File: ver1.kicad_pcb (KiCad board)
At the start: 2 copper layers, 103 x 76 mm, 61 parts, among them P1 CONN_6, P2 CONN_2, P3 CONN_4, P4 CONN_4, P5 CONN_4, P6 USB_Micro_B, U1 MCP1790, U2 STM32F100C6, U3 DRV8833C, U4 DRV8833C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

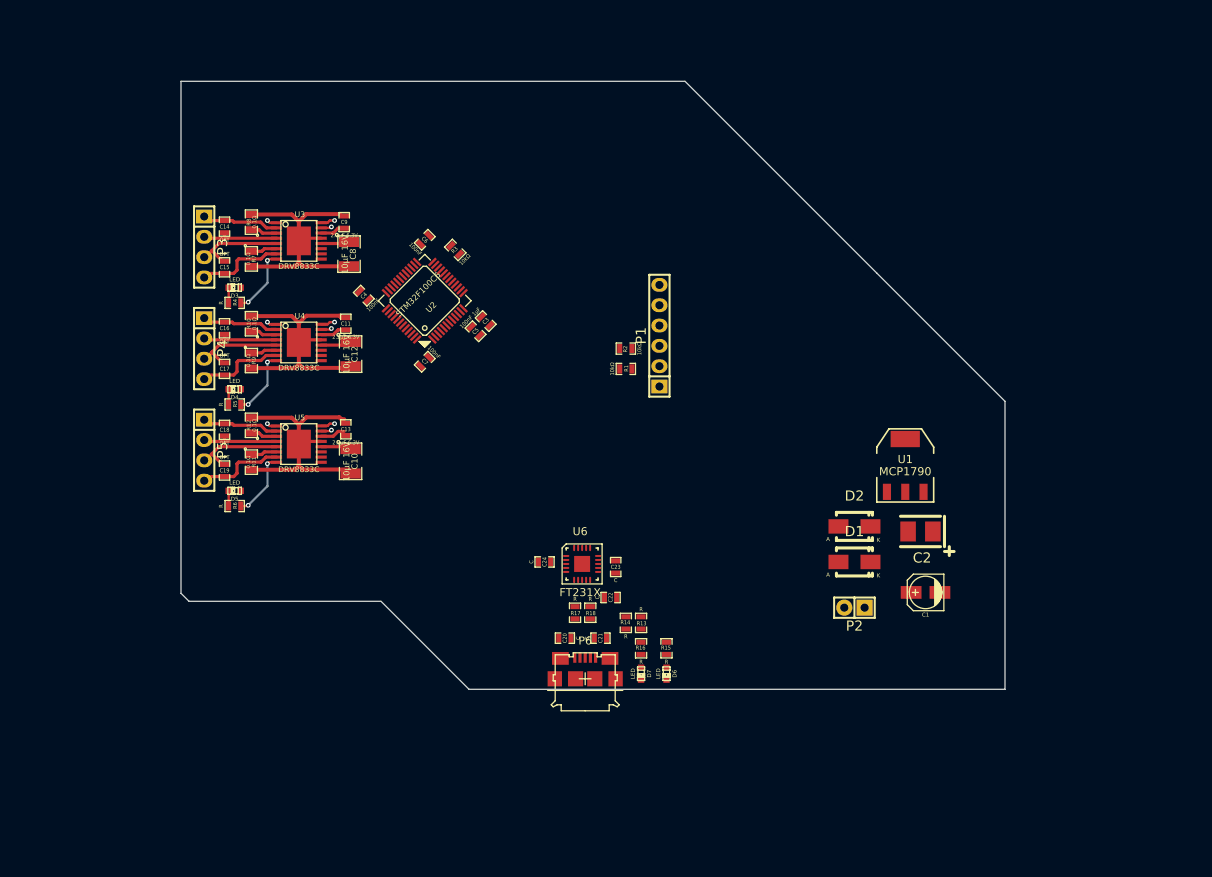
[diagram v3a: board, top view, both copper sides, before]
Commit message: Added PC interface and did some routing
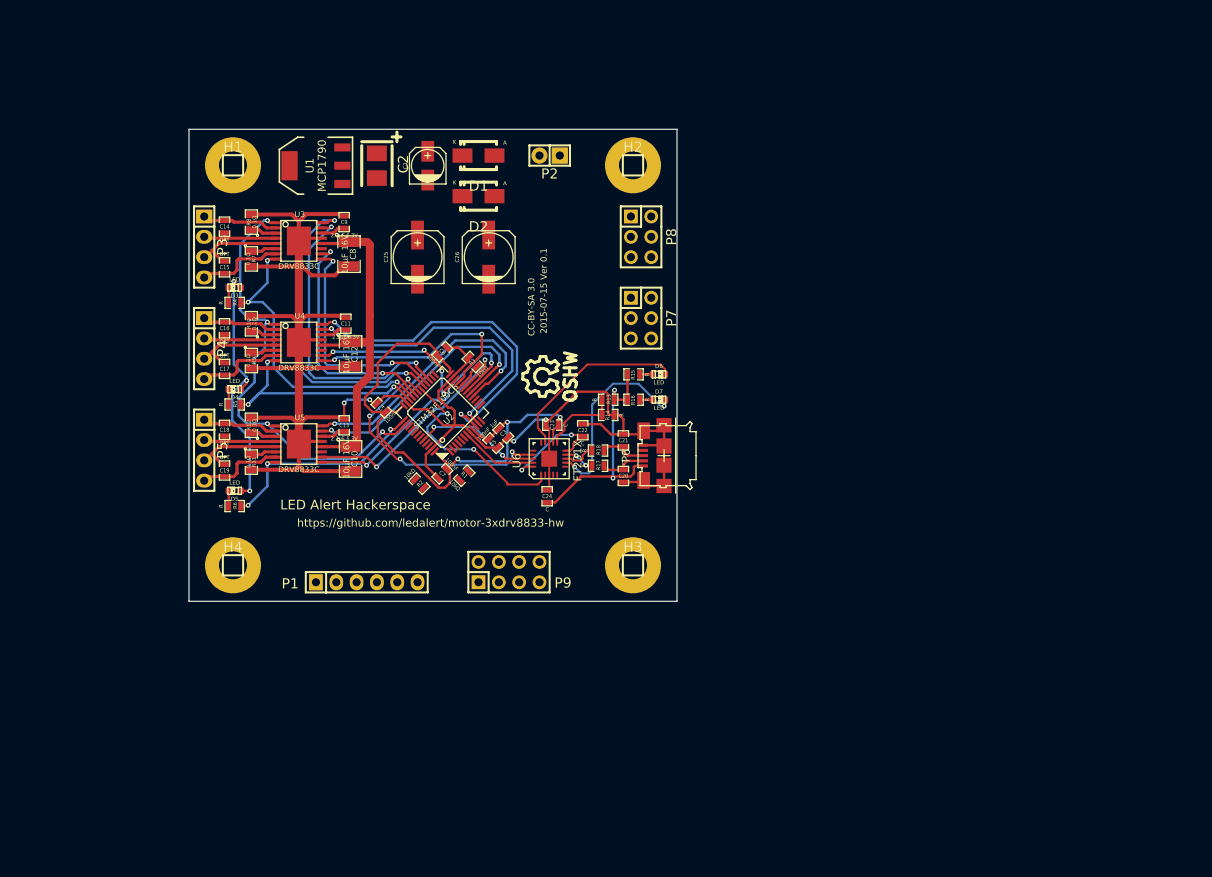
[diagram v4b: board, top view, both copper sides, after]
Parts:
- added C25: 220µF 16V, Capacitors_SMD:c_elec_6.3x7.7, F.Cu at (115.6, 94.0)
- added C26: 220µF 16V, Capacitors_SMD:c_elec_6.3x7.7, F.Cu at (124.5, 94.0)
- added H1: CONN_1, Pin_Headers:Pin_Header_Straight_1x01, F.Cu at (92.5, 82.5)
- added H2: CONN_1, Pin_Headers:Pin_Header_Straight_1x01, F.Cu at (142.5, 82.5)
- added H3: CONN_1, Pin_Headers:Pin_Header_Straight_1x01, F.Cu at (142.5, 132.5)
- added H4: CONN_1, Pin_Headers:Pin_Header_Straight_1x01, F.Cu at (92.5, 132.5)
- added P7: CONN_3X2, Pin_Headers:Pin_Header_Straight_2x03, F.Cu at (143.5, 101.6)
- added P8: CONN_3X2, Pin_Headers:Pin_Header_Straight_2x03, F.Cu at (143.5, 91.4)
- added P9: CONN_4X2, Pin_Headers:Pin_Header_Straight_2x04, F.Cu at (127.0, 133.3)
- added SYM: Symbol_OSHW-Logo_SilkScreen_07Jul2012, Symbols:Symbol_OSHW-Logo_SilkScreen, F.Cu at (131.2, 108.9)
- moved U1 82.6 mm to (102.9, 82.5), turned to 90 degrees
- moved C1 82.0 mm to (116.8, 82.5), turned to 90 degrees
- moved C2 81.9 mm to (110.5, 82.5), turned to 270 degrees
- moved D1 69.2 mm to (123.2, 81.3), turned to 180 degrees
- moved P2 68.2 mm to (132.1, 81.3)
- moved D2 62.5 mm to (123.2, 86.4), turned to 180 degrees
- moved P1 47.8 mm to (109.2, 134.6), turned to 0 degrees
- moved D6 37.4 mm to (145.7, 108.6), turned to 0 degrees
- moved R15 34.5 mm to (142.6, 108.6), turned to 180 degrees
- moved D7 34.3 mm to (145.7, 111.8), turned to 0 degrees
- moved R16 31.1 mm to (142.6, 111.8), turned to 180 degrees
- moved R2 30.8 mm to (115.8, 122.3), turned to 315 degrees
- moved P6 29.6 mm to (146.4, 118.8), turned to 90 degrees
- moved R13 28.2 mm to (139.4, 111.8), turned to 0 degrees
- moved R14 26.1 mm to (139.4, 113.7), turned to 180 degrees
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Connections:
- net Net-(C1-Pad1) renamed /VDD_INT
- U2 pad 12: (no net) -> /ESP8266 PTH Connector/RXD
- U2 pad 13: (no net) -> /ESP8266 PTH Connector/TXD
- U2 pad 14: (no net) -> /GPIO1
- U2 pad 25: (no net) -> /ESP8266 PTH Connector/RST
- U2 pad 26: (no net) -> /ESP8266 PTH Connector/CH_PD
- U2 pad 39: (no net) -> /ESP8266 PTH Connector/GPIO0
- U2 pad 40: (no net) -> /ESP8266 PTH Connector/GPIO2
- U2 pad 42: (no net) -> /GPIO5
- U2 pad 43: (no net) -> /GPIO6
- U2 pad 45: (no net) -> /GPIO7
- U2 pad 46: (no net) -> /GPIO8
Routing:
- net GND: track 99.3 -> 234.5 mm, vias 0 -> 4
- net VCC: track 0.00 -> 105.4 mm, vias 0 -> 6
- net /drv8833_1/SLEEP_IN: track 3.76 -> 59.1 mm, vias 3 -> 4
- net /drv8833_2/AIN1: track 1.79 -> 43.3 mm, vias 1 -> 2
- net /drv8833_1/AIN1: track 1.79 -> 40.1 mm, vias 1 -> 2
- net /drv8833_2/AIN2: track 1.33 -> 38.7 mm, vias 1 -> 2
- net /drv8833_1/AIN2: track 1.33 -> 37.9 mm, vias 1 -> 2
- net /PC Interface/TX: track 0.00 -> 34.2 mm, vias 0 -> 4
- net /drv8833_3/AIN1: track 1.79 -> 35.5 mm, vias 1 -> 2
- net /drv8833_3/BIN1: track 0.00 -> 33.7 mm, vias 0 -> 2
- net /drv8833_3/AIN2: track 1.33 -> 33.7 mm, vias 1 -> 2
- net /PC Interface/VBUS: track 0.00 -> 31.6 mm, vias 0 -> 2
- net /drv8833_3/BIN2: track 0.00 -> 31.6 mm, vias 0 -> 2
- net VDD: track 10.7 -> 42.2 mm
- net /drv8833_1/FAULT_OUT: track 8.37 -> 38.3 mm, vias 2 -> 3
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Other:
- board size 103 x 76 mm -> 61 x 59 mm
- net class Default: clearance 0.2 -> 0.15
- rule trace_clearance: 0.2 -> 0.15
- board text added: "2015-07-15 Ver 0.1"
- board text added: "CC-BY-SA 3.0"
- board text added: "LED Alert Hackerspace"
- board text added: "https://github.com/ledalert/motor-3xdrv8833-hw"

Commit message: Final routing complete
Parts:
- added D8: LED, LEDs:LED-0603, F.Cu at (136.1, 102.5)
- added R19: R, SMD_Packages:SMD-0603_r, F.Cu at (134.3, 102.5)
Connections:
- U1 pad 4: (no net) -> GND
- U2 pad 41: (no net) -> /STATUS_LED
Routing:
- net GND: track 234.5 -> 518.7 mm, vias 4 -> 24
- net VCC: track 105.4 -> 256.5 mm, vias 6 -> 9
- net /STATUS_LED: track 0.00 -> 85.5 mm, vias 0 -> 2
- net /GPIO6: track 0.00 -> 76.0 mm, vias 0 -> 1
- net /GPIO5: track 0.00 -> 71.3 mm, vias 0 -> 1
- net /GPIO7: track 0.00 -> 70.9 mm, vias 0 -> 2
- net VDD: track 42.2 -> 112.3 mm
- net /GPIO8: track 0.00 -> 62.4 mm, vias 0 -> 2
- net /VDD_INT: track 0.00 -> 60.4 mm, vias 0 -> 2
- net /ESP8266 PTH Connector/TXD: track 0.00 -> 51.3 mm, vias 0 -> 2
- net /ESP8266 PTH Connector/CH_PD: track 0.00 -> 49.4 mm, vias 0 -> 4
- net /PC Interface/VBUS: track 31.6 -> 80.1 mm, vias 2 -> 6
- net /ESP8266 PTH Connector/RST: track 0.00 -> 41.5 mm, vias 0 -> 4
- net /PC Interface/RTS: track 9.74 -> 42.1 mm
- net /ESP8266 PTH Connector/GPIO2: track 0.00 -> 31.4 mm, vias 0 -> 1
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- added copper zone on B.Cu, net GND
- added copper zone on F.Cu, net GND
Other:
- board text added: "!Reset"
- board text added: "+"
- board text added: "-"
- board text added: "2015-07-15 Ver 0.2"
- board text added: "3.3V"
- board text added: "Boot"
- board text added: "CC-BY-SA 4.0"
- board text added: "Fault"
- board text added: "GND"
- board text added: "Max 10V"
- board text added: "Rx"
- board text added: "Status"
- board text added: "Tx"
- board text removed: "2015-07-15 Ver 0.1"
- board text removed: "CC-BY-SA 3.0"

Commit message: Final changes for v0.21
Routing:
- net VCC: track 256.5 -> 255.5 mm
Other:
- rule pad_to_mask_clearance: 0 -> 0.05
- board text added: "2015-07-19 Ver 0.21"
- board text removed: "2015-07-15 Ver 0.2"
